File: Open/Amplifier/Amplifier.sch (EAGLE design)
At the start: 14 parts

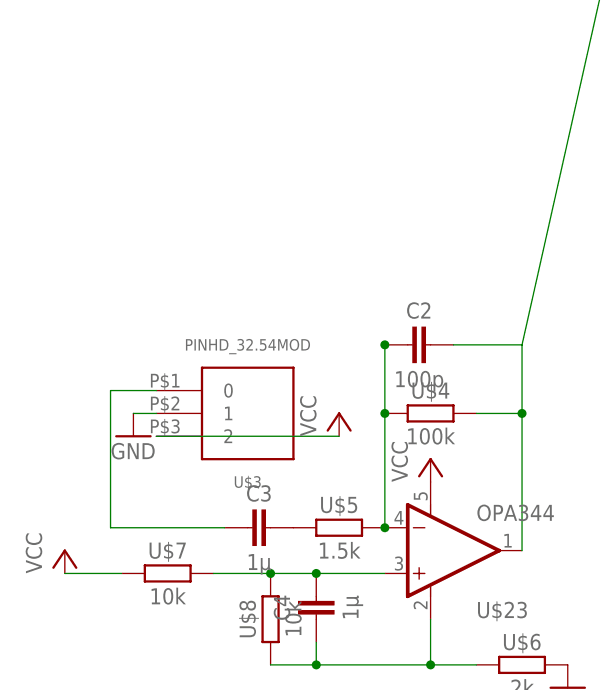
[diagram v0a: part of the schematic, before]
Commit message: Update Pinheader
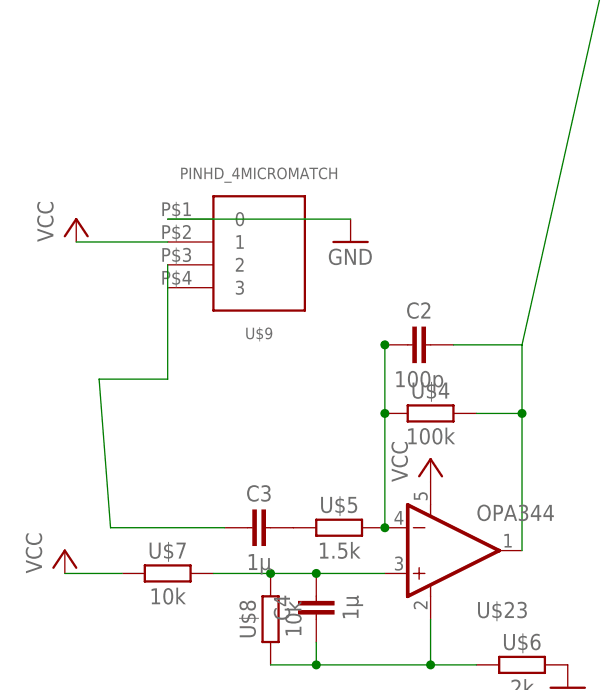
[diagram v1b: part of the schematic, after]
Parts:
- removed U$3: PINHD_32.54MOD, thar:PINHD_32.54MOD
- added U$9: PINHD_4MICROMATCH, thar:PINHD_4MICROMATCH
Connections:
- net GND: now also U$9.0; no longer U$3.1
- net N$56: now also U$9.2, U$9.3; no longer U$3.0
- net VCC: now also U$9.1; no longer U$3.2
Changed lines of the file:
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@@
 <grid distance="0.1" unitdist="inch" unit="inch" style="lines" multiple="1" display="no" altdistance="0.01" altunitdist="inch" altunit="inch"/>
 <layers>
-<layer number="1" name="Top" color="4" fill="1" visible="yes" active="no"/>
-<layer number="16" name="Bottom" color="1" fill="1" visible="yes" active="no"/>
-<layer number="17" name="Pads" color="2" fill="1" visible="yes" active="no"/>
-<layer number="18" name="Vias" color="2" fill="1" visible="yes" active="no"/>
-<layer number="19" name="Unrouted" color="6" fill="1" visible="yes" active="no"/>
-<layer number="20" name="Dimension" color="15" fill="1" visible="yes" active="no"/>
-<layer number="21" name="tPlace" color="7" fill="1" visible="yes" active="no"/>
-<layer number="22" name="bPlace" color="7" fill="1" visible="yes" active="no"/>
-<layer number="23" name="tOrigins" color="15" fill="1" visible="yes" active="no"/>
-<layer number="24" name="bOrigins" color="15" fill="1" visible="yes" active="no"/>
-<layer number="25" name="tNames" color="7" fill="1" visible="yes" active="no"/>
-<layer number="26" name="bNames" color="7" fill="1" visible="yes" active="no"/>
-<layer number="27" name="tValues" color="7" fill="1" visible="yes" active="no"/>
-<layer number="28" name="bValues" color="7" fill="1" visible="yes" active="no"/>
+<layer number="1" name="Top" color="4" fill="1" visible="no" active="no"/>
+<layer number="16" name="Bottom" color="1" fill="1" visible="no" active="no"/>
+<layer number="17" name="Pads" color="2" fill="1" visible="no" active="no"/>
+<layer number="18" name="Vias" color="2" fill="1" visible="no" active="no"/>
+<layer number="19" name="Unrouted" color="6" fill="1" visible="no" active="no"/>
+<layer number="20" name="Dimension" color="15" fill="1" visible="no" active="no"/>
+<layer number="21" name="tPlace" color="7" fill="1" visible="no" active="no"/>
+<layer number="22" name="bPlace" color="7" fill="1" visible="no" active="no"/>
+<layer number="23" name="tOrigins" color="15" fill="1" visible="no" active="no"/>
+<layer number="24" name="bOrigins" color="15" fill="1" visible="no" active="no"/>
+<layer number="25" name="tNames" color="7" fill="1" visible="no" active="no"/>
+<layer number="26" name="bNames" color="7" fill="1" visible="no" active="no"/>
+<layer number="27" name="tValues" color="7" fill="1" visible="no" active="no"/>
+<layer number="28" name="bValues" color="7" fill="1" visible="no" active="no"/>
 <layer number="29" name="tStop" color="7" fill="3" visible="no" active="no"/>
 <layer number="30" name="bStop" color="7" fill="6" visible="no" active="no"/>
@@
 <layer number="35" name="tGlue" color="7" fill="4" visible="no" active="no"/>
 <layer number="36" name="bGlue" color="7" fill="5" visible="no" active="no"/>
-<layer number="37" name="tTest" color="7" fill="1" visible="yes" active="no"/>
-<layer number="38" name="bTest" color="7" fill="1" visible="yes" active="no"/>
+<layer number="37" name="tTest" color="7" fill="1" visible="no" active="no"/>
+<layer number="38" name="bTest" color="7" fill="1" visible="no" active="no"/>
 <layer number="39" name="tKeepout" color="4" fill="11" visible="no" active="no"/>
 <layer number="40" name="bKeepout" color="1" fill="11" visible="no" active="no"/>
@@
 <layer number="44" name="Drills" color="7" fill="1" visible="no" active="no"/>
 <layer number="45" name="Holes" color="7" fill="1" visible="no" active="no"/>
-<layer number="46" name="Milling" color="3" fill="1" visible="yes" active="no"/>
-<layer number="47" name="Measures" color="7" fill="1" visible="yes" active="no"/>
-<layer number="48" name="Document" color="7" fill="1" visible="yes" active="no"/>
-<layer number="49" name="Reference" color="7" fill="1" visible="yes" active="no"/>
-<layer number="50" name="dxf" color="7" fill="1" visible="yes" active="no"/>
-<layer number="51" name="tDocu" color="7" fill="1" visible="yes" active="no"/>
-<layer number="52" name="bDocu" color="7" fill="1" visible="yes" active="no"/>
-<layer number="53" name="tGND_GNDA" color="7" fill="9" visible="yes" active="no"/>
-<layer number="54" name="bGND_GNDA" color="1" fill="9" visible="yes" active="no"/>
-<layer number="56" name="wert" color="7" fill="1" visible="yes" active="no"/>
-<layer number="57" name="tCAD" color="7" fill="1" visible="yes" active="no"/>
+<layer number="46" name="Milling" color="3" fill="1" visible="no" active="no"/>
+<layer number="47" name="Measures" color="7" fill="1" visible="no" active="no"/>
+<layer number="48" name="Document" color="7" fill="1" visible="no" active="no"/>
+<layer number="49" name="Reference" color="7" fill="1" visible="no" active="no"/>
+<layer number="50" name="dxf" color="7" fill="1" visible="no" active="no"/>
+<layer number="51" name="tDocu" color="7" fill="1" visible="no" active="no"/>
+<layer number="52" name="bDocu" color="7" fill="1" visible="no" active="no"/>
+<layer number="53" name="tGND_GNDA" color="7" fill="9" visible="no" active="no"/>
+<layer number="54" name="bGND_GNDA" color="1" fill="9" visible="no" active="no"/>
+<layer number="56" name="wert" color="7" fill="1" visible="no" active="no"/>
+<layer number="57" name="tCAD" color="7" fill="1" visible="no" active="no"/>
+<layer number="90" name="Modules" color="5" fill="1" visible="no" active="no"/>
 <layer number="91" name="Nets" color="2" fill="1" visible="yes" active="yes"/>
 <layer number="92" name="Busses" color="1" fill="1" visible="yes" active="yes"/>
@@
 <part name="GND6" library="supply1" deviceset="GND" device=""/>
 <part name="U$23" library="SparkFun-AnalogIC" deviceset="OPA344" device=""/>
-<part name="P+2" library="supply1" deviceset="VCC" device=""/>
-<part name="GND2" library="supply1" deviceset="GND" device=""/>
 <part name="P+7" library="supply1" deviceset="VCC" device=""/>
 <part name="GND4" library="supply1" deviceset="GND" device=""/>
@@
 <part name="P+1" library="supply1" deviceset="VCC" device=""/>
 <part name="GND7" library="supply1" deviceset="GND" device=""/>
-<part name="U$3" library="thar" deviceset="PINHD_3" device="2.54MOD"/>
+<part name="U$9" library="thar" deviceset="PINHD_4" device="MICROMATCH"/>
+<part name="P+8" library="supply1" deviceset="VCC" device=""/>
+<part name="GND2" library="supply1" deviceset="GND" device=""/>
 </parts>
 <sheets>
@@
 <instance part="GND6" gate="1" x="71.12" y="96.52"/>
 <instance part="U$23" gate="G$1" x="52.07" y="29.21"/>
-<instance part="P+2" gate="VCC" x="41.91" y="44.45"/>
-<instance part="GND2" gate="1" x="19.05" y="41.91"/>
 <instance part="P+7" gate="VCC" x="52.07" y="39.37"/>
 <instance part="GND4" gate="1" x="67.31" y="13.97"/>
@@
 <instance part="P+1" gate="VCC" x="152.4" y="106.68"/>
 <instance part="GND7" gate="1" x="144.78" y="104.14"/>
-<instance part="U$3" gate="G$1" x="31.75" y="44.45"/>
+<instance part="U$9" gate="G$1" x="33.02" y="63.5"/>
+<instance part="P+8" gate="VCC" x="12.7" y="66.04"/>
+<instance part="GND2" gate="1" x="43.18" y="63.5"/>
 </instances>
 <busses>
@@
 </segment>
 <segment>
-<pinref part="GND2" gate="1" pin="GND"/>
-<pinref part="U$3" gate="G$1" pin="1"/>
-<wire x1="19.05" y1="44.45" x2="21.59" y2="44.45" width="0.1524" layer="91"/>
-</segment>
-<segment>
 <pinref part="U$1" gate="A" pin="V_A"/>
 <pinref part="GND7" gate="1" pin="GND"/>
 <wire x1="144.78" y1="106.68" x2="157.48" y2="106.68" width="0.1524" layer="91"/>
+</segment>
+<segment>
+<pinref part="U$9" gate="G$1" pin="0"/>
+<pinref part="GND2" gate="1" pin="GND"/>
+<wire x1="43.18" y1="66.04" x2="22.86" y2="66.04" width="0.1524" layer="91"/>
 </segment>
 </net>
@@
 </segment>
 <segment>
-<pinref part="P+2" gate="VCC" pin="VCC"/>
-<wire x1="41.91" y1="41.91" x2="21.59" y2="41.91" width="0.1524" layer="91"/>
-<pinref part="U$3" gate="G$1" pin="2"/>
-</segment>
-<segment>
 <pinref part="U$1" gate="A" pin="V_B"/>
 <pinref part="P+1" gate="VCC" pin="VCC"/>
 <wire x1="152.4" y1="104.14" x2="157.48" y2="104.14" width="0.1524" layer="91"/>
+</segment>
+<segment>
+<pinref part="U$9" gate="G$1" pin="1"/>
+<pinref part="P+8" gate="VCC" pin="VCC"/>
+<wire x1="12.7" y1="63.5" x2="22.86" y2="63.5" width="0.1524" layer="91"/>
 </segment>
 </net>
@@
 <segment>
 <wire x1="29.21" y1="31.75" x2="16.51" y2="31.75" width="0.1524" layer="91"/>
-<wire x1="16.51" y1="46.99" x2="16.51" y2="31.75" width="0.1524" layer="91"/>
-<wire x1="21.59" y1="46.99" x2="16.51" y2="46.99" width="0.1524" layer="91"/>
+<wire x1="15.24" y1="48.26" x2="16.51" y2="31.75" width="0.1524" layer="91"/>
 <pinref part="C3" gate="G$1" pin="1"/>
-<pinref part="U$3" gate="G$1" pin="0"/>
-</segment>
-</net>
+<pinref part="U$9" gate="G$1" pin="3"/>
+<wire x1="15.24" y1="48.26" x2="22.86" y2="48.26" width="0.1524" layer="91"/>
+<wire x1="22.86" y1="48.26" x2="22.86" y2="58.42" width="0.1524" layer="91"/>
+<pinref part="U$9" gate="G$1" pin="2"/>
+<wire x1="22.86" y1="58.42" x2="22.86" y2="60.96" width="0.1524" layer="91"/>
+</segment>
+</net>
